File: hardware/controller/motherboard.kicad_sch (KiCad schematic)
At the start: 53 parts, among them J10 TC2030, J2 Molex PicoBlade, J3 Conn_02x06_Odd_Even, J4 AFB10-S18LCA-00, J5 726386-2, J6 Conn_Coaxial_Small, J7 AFB10-S06LCA-00, J9 PinHeader 1x10 P1.00mm, Q1 AO3401A, SW1 SW_Push, U1 nRF52840-QIAA, U2 nPM1300-QEAA, Y1 32MHz, Y2 32.768 kHz

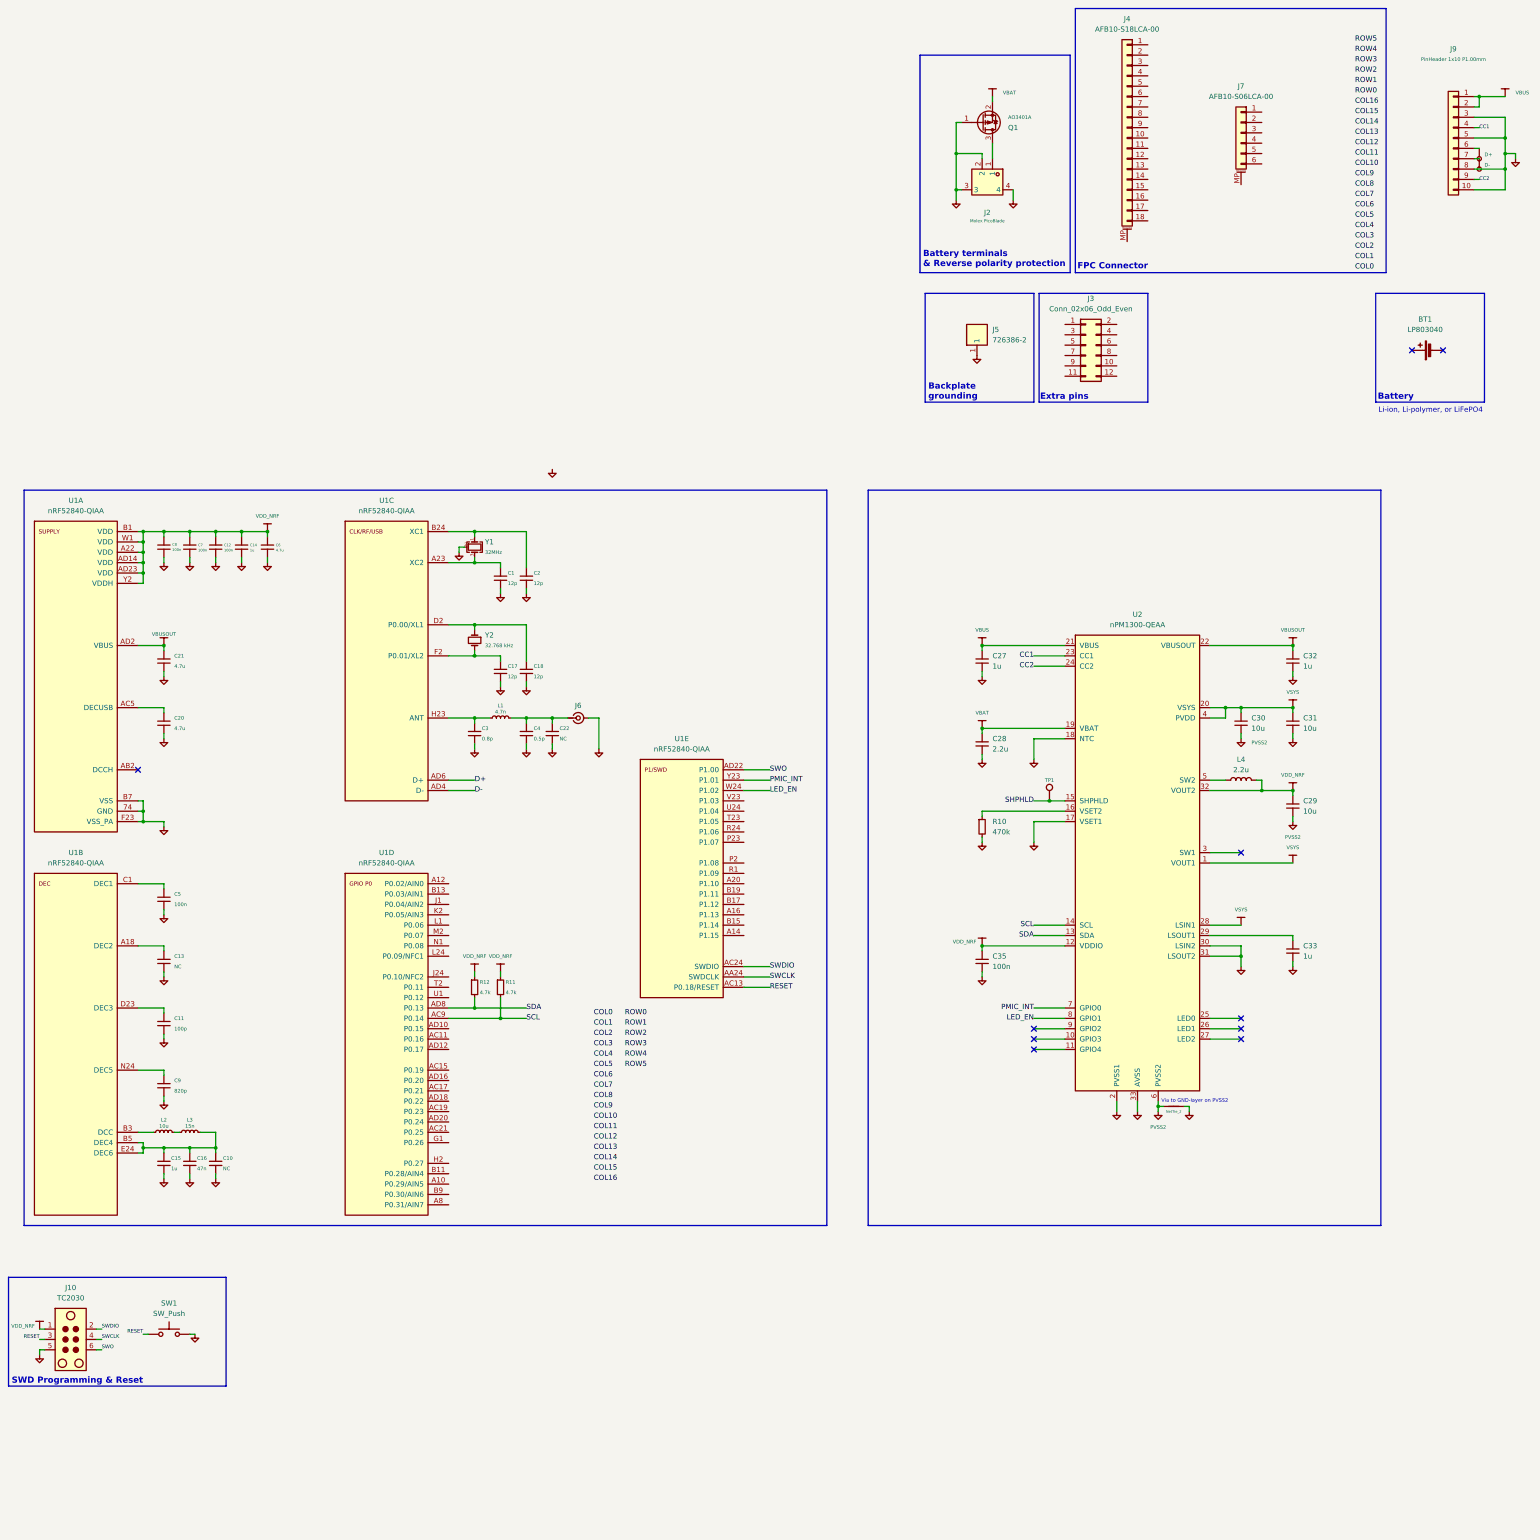
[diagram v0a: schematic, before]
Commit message: feat(controller): matrix COL0-16/ROW0-5 on nRF52840 and J4/J7
Provisional pin assignment per HARDWARE_DECISIONS side split; to be
reshuffled during routing. J4 pin 18 and J4/J7 mounting pads on GND.
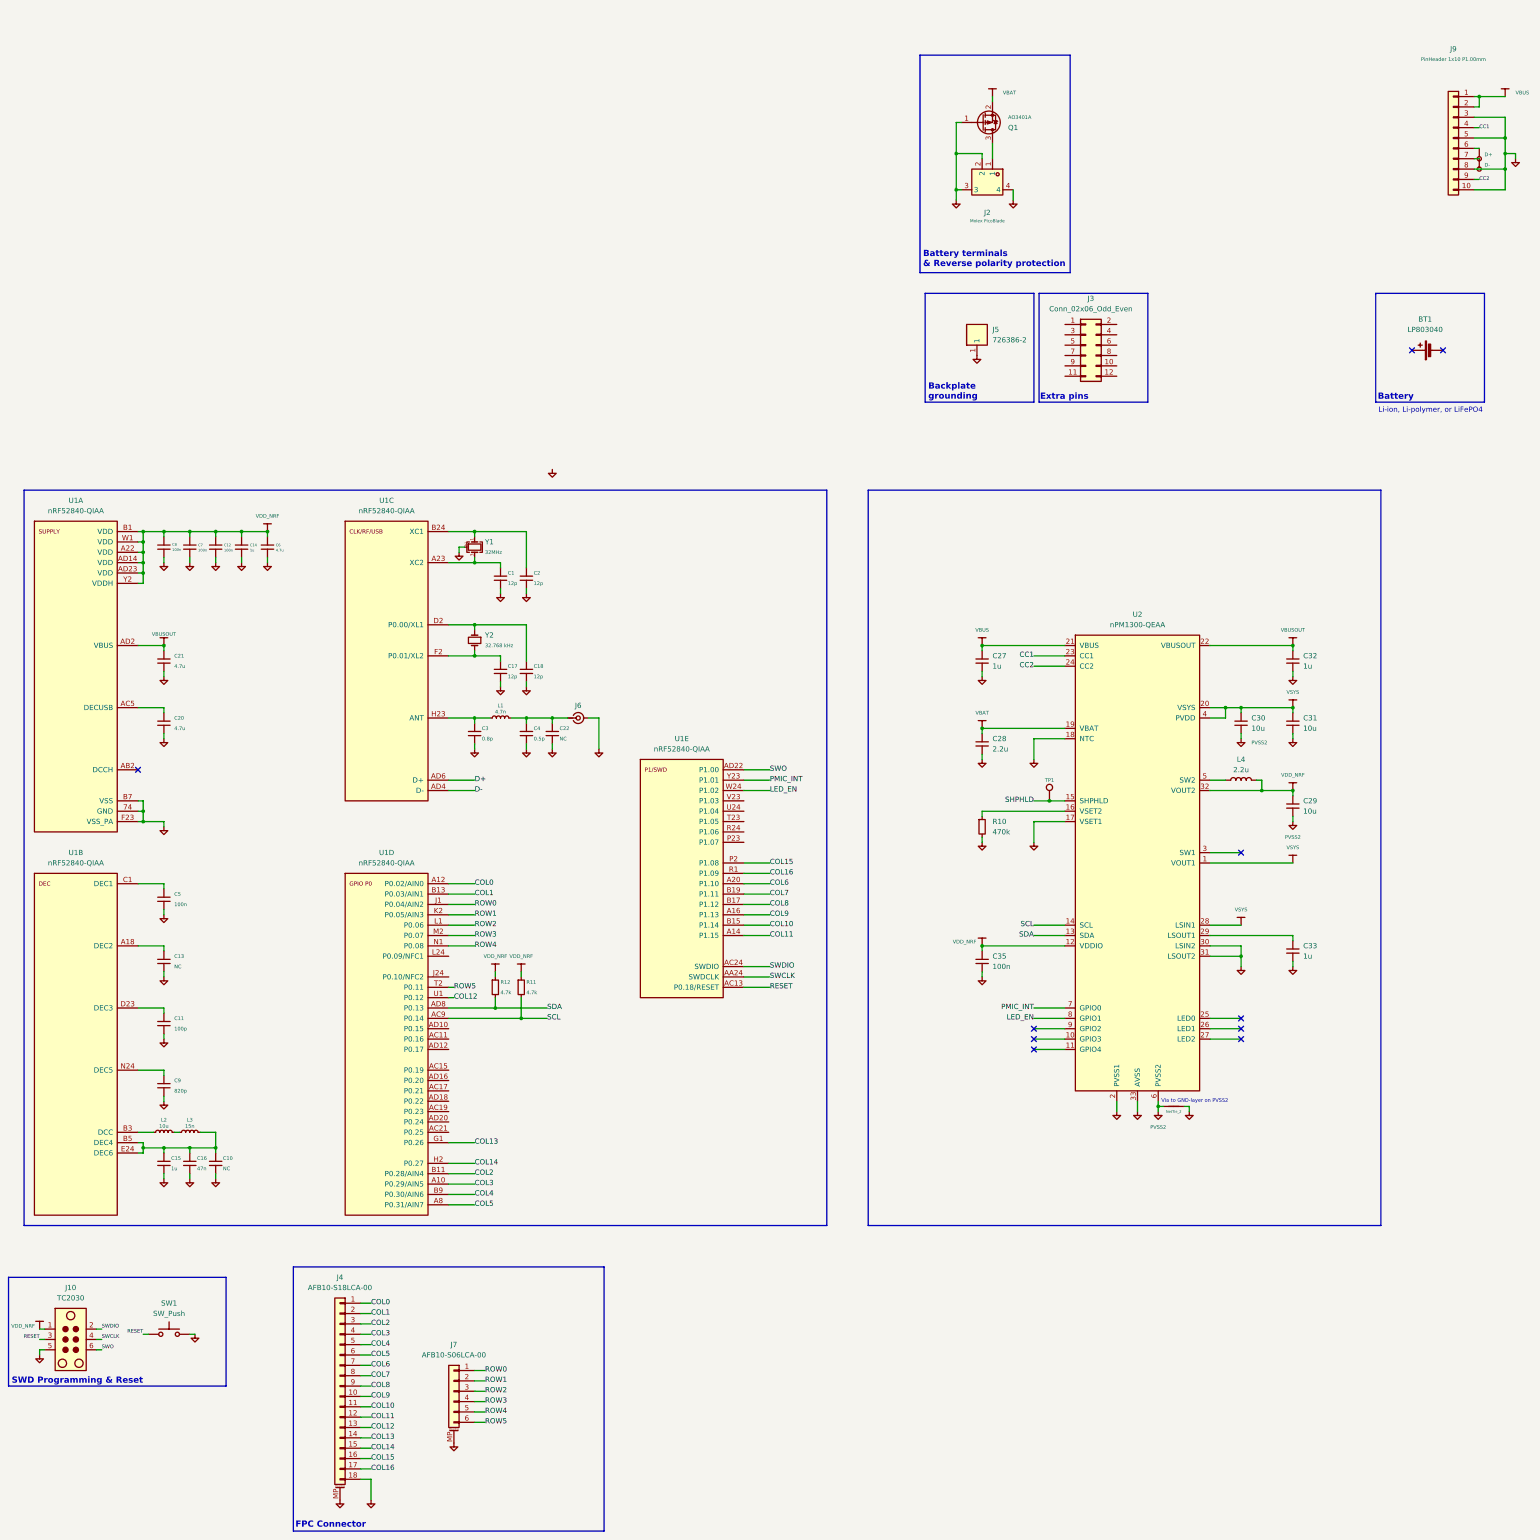
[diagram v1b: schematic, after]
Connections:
- net COL0: now also J4.1 (Pin_1), U1.A12 (P0.02/AIN0)
- net COL1: now also J4.2 (Pin_2), U1.B13 (P0.03/AIN1)
- net COL10: now also J4.11 (Pin_11), U1.B15 (P1.14)
- net COL11: now also J4.12 (Pin_12), U1.A14 (P1.15)
- net COL12: now also J4.13 (Pin_13), U1.U1 (P0.12)
- net COL13: now also J4.14 (Pin_14), U1.G1 (P0.26)
- net COL14: now also J4.15 (Pin_15), U1.H2 (P0.27)
- net COL15: now also J4.16 (Pin_16), U1.P2 (P1.08)
- net COL16: now also J4.17 (Pin_17), U1.R1 (P1.09)
- net COL2: now also J4.3 (Pin_3), U1.B11 (P0.28/AIN4)
- net COL3: now also J4.4 (Pin_4), U1.A10 (P0.29/AIN5)
- net COL4: now also J4.5 (Pin_5), U1.B9 (P0.30/AIN6)
- net COL5: now also J4.6 (Pin_6), U1.A8 (P0.31/AIN7)
- net COL6: now also J4.7 (Pin_7), U1.A20 (P1.10)
- net COL7: now also J4.8 (Pin_8), U1.B19 (P1.11)
- net COL8: now also J4.9 (Pin_9), U1.B17 (P1.12)
- net COL9: now also J4.10 (Pin_10), U1.A16 (P1.13)
- net GND: now also J4.18 (Pin_18), J4.MP (MountPin), J7.MP (MountPin)
- net ROW0: now also J7.1 (Pin_1), U1.J1 (P0.04/AIN2)
- net ROW1: now also J7.2 (Pin_2), U1.K2 (P0.05/AIN3)
- net ROW2: now also J7.3 (Pin_3), U1.L1 (P0.06)
- net ROW3: now also J7.4 (Pin_4), U1.M2 (P0.07)
- net ROW4: now also J7.5 (Pin_5), U1.N1 (P0.08)
- net ROW5: now also J7.6 (Pin_6), U1.T2 (P0.11)
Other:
- moved on the sheet: J4, J7, R11, R12

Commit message: feat(controller): status LED D2 on MB (I2)
WS2812C-2020 on VLED (LOADSW1 output) with C19, DIN from P0.15 via
RGB_DIN, DOUT unconnected. Changelog: I2 applied.
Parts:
- added C19: 100n, Package_SON:WSON-8-1EP_6x5mm_P1.27mm_EP3.4x4mm, symbol Device:C_Small
- added D2: rgb, LED_SMD:LED_WS2812B-2020_PLCC4_2.0x2.0mm, symbol easyeda2kicad:rgb
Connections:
- net GND: now also C19.2, D2.2 (VSS)
- net RGB_DIN: now reaches U1.AD10 (P0.15)
- net RGB_DIN: now also D2.3 (DIN)
- net VLED: now reaches C33.1, U2.29 (LSOUT1)
- net VLED: now also C19.1, D2.4 (VDD)
- no-connect marks 10 -> 11
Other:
- moved on the sheet: J10, J3, J4, J7, SW1

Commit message: feat(controller): expansion connector J3 as 2x3 1.27 mm SMD header (S3)
VSYS, VDD_NRF, GND, EXT_INT (P0.19), SCL, SDA. Replaces the 2x6
layout from S1; HARDWARE_DECISIONS updated.
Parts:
- removed J3: Conn_02x06_Odd_Even, symbol Connector_Generic:Conn_02x06_Odd_Even
- added J3: Conn_02x03_Counter_Clockwise, Connector_PinHeader_1.27mm:PinHeader_2x03_P1.27mm_Vertical_SMD, symbol Connector_Generic:Conn_02x03_Odd_Even
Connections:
- net GND: now also J3.3 (Pin_3)
- net SCL: now also J3.5 (Pin_5)
- net SDA: now also J3.6 (Pin_6)
- net VDD_NRF: now also J3.2 (Pin_2)
- net VSYS: now also J3.1 (Pin_1)
- net EXT_INT: now reaches U1.AC15 (P0.19)
- net EXT_INT: now also J3.4 (Pin_4)
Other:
- note added: "Expansion connector"
- note removed: "Extra pins"
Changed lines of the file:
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@@
 	(rectangle
 		(start 186.69 198.12)
-		(end 213.36 224.79)
+		(end 222.25 224.79)
 		(stroke
 			(width 0.1905)
@@
 		)
 	)
-	(text "Extra pins"
+	(text "Expansion connector"
 		(exclude_from_sim no)
 		(at 186.944 223.52 0)
@@
 	(wire
 		(pts
+			(xy 195.58 208.28) (xy 196.85 208.28)
+		)
+		(stroke
+			(width 0)
+			(type default)
+		)
+	)
+	(wire
+		(pts
 			(xy 152.4 121.92) (xy 158.75 121.92)
 		)
@@
 	(wire
 		(pts
+			(xy 195.58 213.36) (xy 196.85 213.36)
+		)
+		(stroke
+			(width 0)
+			(type default)
+		)
+	)
+	(wire
+		(pts
 			(xy 339.09 86.36) (xy 342.9 86.36)
 		)
@@
 	(wire
 		(pts
+			(xy 209.55 213.36) (xy 210.82 213.36)
+		)
+		(stroke
+			(width 0)
+			(type default)
+		)
+	)
+	(wire
+		(pts
+			(xy 152.4 157.48) (xy 158.75 157.48)
+		)
+		(stroke
+			(width 0)
+			(type default)
+		)
+	)
+	(wire
+		(pts
 			(xy 359.41 124.46) (xy 359.41 125.73)
 		)
@@
 	(wire
 		(pts
+			(xy 209.55 208.28) (xy 210.82 208.28)
+		)
+		(stroke
+			(width 0)
+			(type default)
+		)
+	)
+	(wire
+		(pts
 			(xy 359.41 74.93) (xy 359.41 76.2)
 		)
@@
 	(wire
 		(pts
+			(xy 209.55 210.82) (xy 210.82 210.82)
+		)
+		(stroke
+			(width 0)
+			(type default)
+		)
+	)
+	(wire
+		(pts
 			(xy 76.2 177.8) (xy 77.47 177.8)
 		)
@@
 	(wire
 		(pts
+			(xy 195.58 210.82) (xy 196.85 210.82)
+		)
+		(stroke
+			(width 0)
+			(type default)
+		)
+	)
+	(wire
+		(pts
 			(xy 171.45 39.37) (xy 171.45 40.64)
 		)
@@
 		)
 	)
+	(label "EXT_INT"
+		(at 210.82 210.82 0)
+		(effects
+			(font
+				(size 1.27 1.27)
+			)
+			(justify left)
+		)
+	)
 	(label "RESET"
 		(at 135.89 213.36 180)
@@
 		)
 	)
+	(label "VDD_NRF"
+		(at 210.82 208.28 0)
+		(effects
+			(font
+				(size 1.27 1.27)
+			)
+			(justify left)
+		)
+	)
 	(label "ROW4"
 		(at 158.75 127 0)
@@
 		)
 	)
+	(label "EXT_INT"
+		(at 158.75 157.48 0)
+		(effects
+			(font
+				(size 1.27 1.27)
+			)
+			(justify left)
+		)
+	)
 	(label "COL5"
 		(at 158.75 190.5 0)
@@
 		)
 	)
+	(label "SCL"
+		(at 195.58 213.36 180)
+		(effects
+			(font
+				(size 1.27 1.27)
+			)
+			(justify right)
+		)
+	)
 	(label "PMIC_INT"
 		(at 295.91 142.24 180)
@@
 		)
 	)
+	(label "GND"
+		(at 195.58 210.82 180)
+		(effects
+			(font
+				(size 1.27 1.27)
+			)
+			(justify right)
+		)
+	)
 	(label "COL11"
 		(at 231.14 124.46 0)
@@
 		)
 	)
+	(label "SDA"
+		(at 210.82 213.36 0)
+		(effects
+			(font
+				(size 1.27 1.27)
+			)
+			(justify left)
+		)
+	)
 	(label "ROW1"
 		(at 158.75 119.38 0)
@@
 		)
 	)
+	(label "VSYS"
+		(at 195.58 208.28 180)
+		(effects
+			(font
+				(size 1.27 1.27)
+			)
+			(justify right)
+		)
+	)
 	(label "COL2"
 		(at 158.75 182.88 0)
@@
 	)
 	(symbol
+		(lib_id "Connector_Generic:Conn_02x03_Odd_Even")
+		(at 201.93 210.82 0)
+		(unit 1)
+		(body_style 1)
+		(exclude_from_sim no)
+		(in_bom yes)
+		(on_board yes)
+		(in_pos_files yes)
+		(dnp no)
+		(fields_autoplaced yes)
+		(property "Reference" "J3"
+			(at 203.2 201.93 0)
+			(show_name no)
+			(do_not_autoplace no)
+			(effects
+				(font
+					(size 1.27 1.27)
+				)
+			)
+		)
+		(property "Value" "Conn_02x03_Counter_Clockwise"
+			(at 203.2 204.47 0)
+			(show_name no)
+			(do_not_autoplace no)
+			(effects
+				(font
+					(size 1.27 1.27)
+				)
+			)
+		)
+		(property "Footprint" "Connector_PinHeader_1.27mm:PinHeader_2x03_P1.27mm_Vertical_SMD"
+			(at 201.93 210.82 0)
+			(hide yes)
+			(show_name no)
+			(do_not_autoplace no)
+			(effects
+				(font
+					(size 1.27 1.27)
+				)
+			)
+		)
+		(property "Datasheet" ""
+			(at 201.93 210.82 0)
+			(hide yes)
+			(show_name no)
+			(do_not_autoplace no)
+			(effects
+				(font
+					(size 1.27 1.27)
+				)
+			)
+		)
+		(property "Description" "Generic connector, double row, 02x03, odd/even pin numbering scheme (row 1 odd numbers, row 2 even numbers), script generated (kicad-library-utils/schlib/autogen/connector/)"
+			(at 201.93 210.82 0)
+			(hide yes)
+			(show_name no)
+			(do_not_autoplace no)
+			(effects
+				(font
+					(size 1.27 1.27)
+				)
+			)
+		)
+		(pin "4"
+		)
+		(pin "3"
+		)
+		(pin "1"
+		)
+		(pin "2"
+		)
+		(pin "5"
+		)
+		(pin "6"
+		)
+		(instances
+			(project "controller"
+				(path "/17f6a4a5-fbff-4e30-a1cc-9481373e4968/0f3c1877-5271-448c-b354-c4d8810124ff"
+					(reference "J3")
+					(unit 1)
+				)
+			)
+		)
+	)
+	(symbol
 		(lib_id "easyeda2kicad:vbus")
 		(at 163.83 133.35 0)
@@
 					(unit 1)
 				)
-			)
-		)
-	)
-	(symbol
-		(lib_id "Connector_Generic:Conn_02x06_Odd_Even")
-		(at 198.12 210.82 0)
-		(unit 1)
-		(body_style 1)
-		(exclude_from_sim no)
-		(in_bom yes)
-		(on_board yes)
-		(in_pos_files yes)
-		(dnp no)
-		(fields_autoplaced yes)
-		(property "Reference" "J3"
-			(at 199.39 199.39 0)
-			(show_name no)
-			(do_not_autoplace no)
-			(effects
-				(font
-					(size 1.27 1.27)
-				)
-			)
-		)
-		(property "Value" "Conn_02x06_Odd_Even"
-			(at 199.39 201.93 0)
-			(show_name no)
-			(do_not_autoplace no)
-			(effects
-				(font
-					(size 1.27 1.27)
-				)
-			)
-		)
-		(property "Footprint" ""
-			(at 198.12 210.82 0)
-			(hide yes)
-			(show_name no)
-			(do_not_autoplace no)
-			(effects
-				(font
-					(size 1.27 1.27)
-				)
-			)
-		)
-		(property "Datasheet" ""
-			(at 198.12 210.82 0)
-			(hide yes)
-			(show_name no)
-			(do_not_autoplace no)
-			(effects
-				(font
-					(size 1.27 1.27)
-				)
-			)
-		)
-		(property "Description" "Generic connector, double row, 02x06, odd/even pin numbering scheme (row 1 odd numbers, row 2 even numbers), script generated (kicad-library-utils/schlib/autogen/connector/)"
-			(at 198.12 210.82 0)
-			(hide yes)
-			(show_name no)
-			(do_not_autoplace no)
-			(effects
-				(font
-					(size 1.27 1.27)
-				)
-			)
-		)
-		(pin "7"
-		)
-		(pin "4"
-		)
-		(pin "6"
-		)
-		(pin "10"
-		)
-		(pin "5"
-		)
-		(pin "1"
-		)
-		(pin "12"
-		)
-		(pin "11"
-		)
-		(pin "3"
-		)
-		(pin "8"
-		)
-		(pin "9"
-		)
-		(pin "2"
-		)
-		(instances
-			(project "controller"
-				(path "/17f6a4a5-fbff-4e30-a1cc-9481373e4968/0f3c1877-5271-448c-b354-c4d8810124ff"
-					(reference "J3")
-					(unit 1)
-				)
